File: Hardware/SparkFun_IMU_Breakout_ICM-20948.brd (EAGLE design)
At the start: 25.4 x 25.4 mm, 79 parts, among them U1 TXB0108DQSR, U2 9DoF IMU, U3 1.8V/100mA

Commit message: Swap TXB0108 for TXS0108 - still needs last check, design review, and finalization
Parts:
- removed U$3: (no value), buzzard_labels_2:GND4
- added U$30, U$44: (no value), buzzard_labels_2:VIN5
- U1: value TXB0108DQSR -> -VFQFN_20; device SparkFun-IC-Comms:UFDFN-20 -> SparkFun-IC-Comms:VFQFN-20
- moved C3 5.76 mm to (7.92, 12.7), turned to 90 degrees
- moved U1 0.89 mm to (12.7, 7.24)
- moved JP4 0.77 mm to (15.7, 7.87)
- moved U$25 0.77 mm to (15.7, 8.38)
- moved C1 0.51 mm to (9.40, 12.7)
- moved R1 0.38 mm to (18.3, 19.2)
- moved R3 0.38 mm to (19.8, 19.2)
- moved R5 0.38 mm to (7.11, 19.2)
- moved R6 0.38 mm to (5.59, 19.2)
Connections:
- net 1.8V: now also U1.10, U1.2; no longer U1.5, U1.6
- net AD0/SDO: now also U1.3; no longer U1.2
- net AD0/SDO_VIN: now also U1.18; no longer U1.19
- net AUX_CL: now also U1.7; no longer U1.8
- net AUX_CL_VIN: now also U1.14; no longer U1.13
- net AUX_DA: now also U1.6; no longer U1.7
- net AUX_DA_VIN: now also U1.15; no longer U1.14
- net FSYNC: now also U1.8; no longer U1.9
- net FSYNC_VIN: now also U1.13; no longer U1.12
- net GND: now also U1.11; no longer J4.6, U1.15
- net INT: now also U1.9; no longer U1.10
- net INT_VIN: now also U1.12; no longer U1.11
- net SCL/SCLK: now also U1.4; no longer U1.3
- net SCL/SCLK_VIN: now also U1.17; no longer U1.18
- net SDA/SDI: now also U1.5; no longer U1.4
- net SDA/SDI_VIN: now also U1.16; no longer U1.17
- net VIN: now also J4.6, U1.19; no longer U1.16
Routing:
- net VIN: track 72.7 -> 82.9 mm, vias 7 -> 6
- net FSYNC: track 12.0 -> 4.90 mm
- net AD0/SDO: track 13.7 -> 7.35 mm
- net GND: track 17.5 -> 11.8 mm, vias 26 -> 29
- net !CS: track 19.1 -> 13.7 mm
- net N$1: track 2.00 -> 7.02 mm
- net INT: track 11.0 -> 8.04 mm
- net AUX_DA: track 18.0 -> 20.3 mm
- net AD0/SDO_VIN: track 18.8 -> 20.5 mm, vias 1 -> 3
- net SCL/SCLK_VIN: track 37.2 -> 35.6 mm, vias 1 -> 3
- net AUX_CL: track 11.0 -> 9.42 mm
- net !CS!_VIN: track 22.5 -> 23.9 mm, vias 4 -> 2
- net SDA/SDI: track 20.1 -> 21.2 mm, vias 2 -> 0
- net 1.8V: track 35.5 -> 36.2 mm, vias 4 -> 3
- net AUX_CL_VIN: track 39.9 -> 40.4 mm
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
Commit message: v20
v20 is intended to fix the I2C communications. We've identified that the TXB0108 logic level translation IC was unable to drive open-drain busses. To address this we've replaced that IC with the TXS0108 - a very similar chip that IS able to drive open-drain busses.
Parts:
- added TP1: 1.8V, SparkFun-Connectors:PAD.03X.03
- U1: value -VFQFN_20 -> TXS0108
- moved C4 0.13 mm to (12.7, 16.6)
- moved U3 0.13 mm to (12.7, 18.7)
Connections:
- net 1.8V: now also TP1.P$1
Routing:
- net !CS!_VIN: track 23.9 -> 22.6 mm
- net SDA/SDI_VIN: track 39.7 -> 38.5 mm, vias 3 -> 4
- net SCL/SCLK_VIN: track 35.6 -> 36.3 mm
- net SDA/SDI: track 21.2 -> 20.5 mm
- net SCL/SCLK: track 18.7 -> 18.1 mm
- net GND: track 11.8 -> 11.9 mm, vias 29 -> 33
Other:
- board text added: "v20"
- board text removed: "v10"

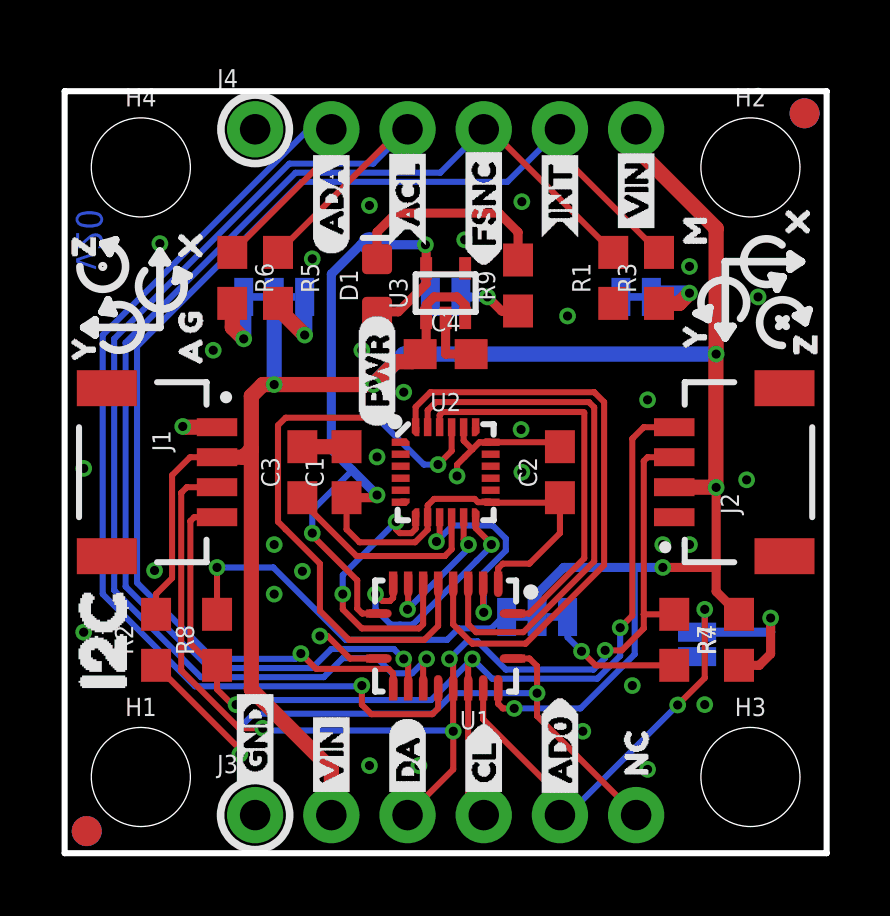
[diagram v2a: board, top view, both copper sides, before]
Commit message: Post design review changes for v20
- PWR silk changed to text only
- Moved P1 indicator on ICM-20948
- I<sup>2<\sup>C
- AD0 -> ADR
- No more '0' label for ADR
- Vin range double checked
- GND label on top left
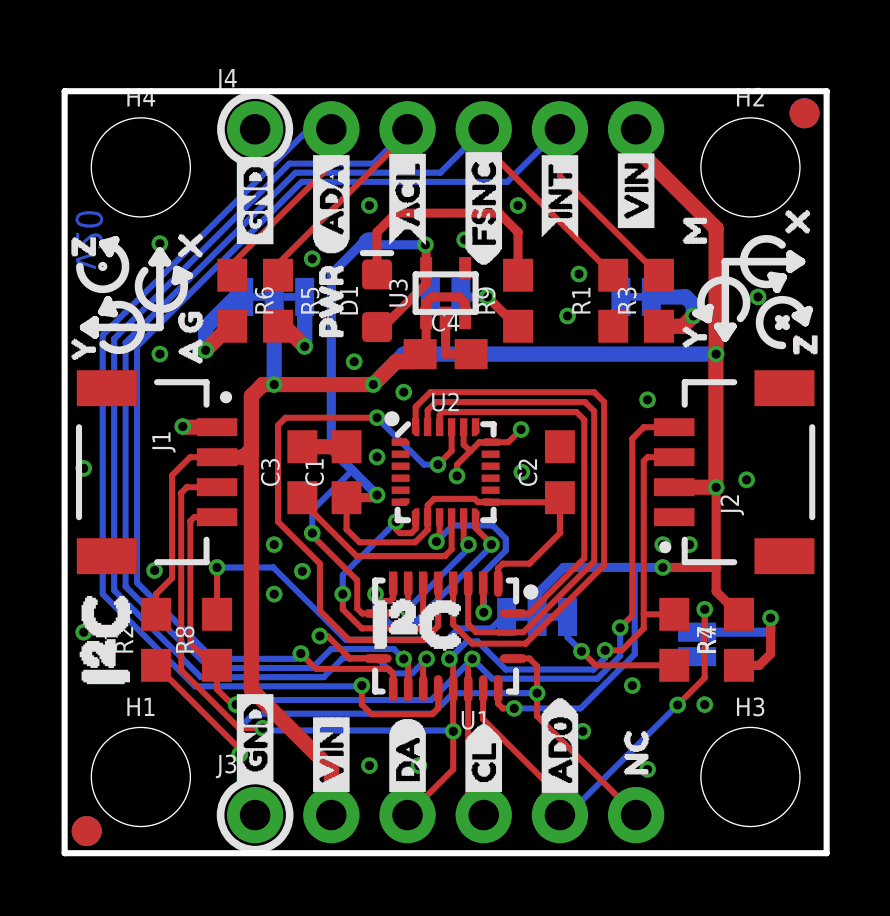
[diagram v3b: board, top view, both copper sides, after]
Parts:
- removed U$32: (no value), buzzard_labels_2:#0#25
- added U$3: (no value), buzzard_labels_4:PWR0
- added U$45: (no value), buzzard_labels_4:I#C1
- JP2: value AD0 -> ADR
- U$23: device buzzard_labels_2:I2C18 -> buzzard_labels_4:ADR2
- U$24: device buzzard_labels_2:AD020 -> buzzard_labels_2:GND4
- U$33: device buzzard_labels (1):PWR0 -> buzzard_labels_4:I#C1
- moved U$23 20.1 mm to (21.1, 7.49), flipped to the bottom
- moved U$24 19.2 mm to (6.35, 19.9), flipped to the top
- moved U$33 6.75 mm to (8.89, 7.62), turned to 0 degrees
- moved R1 0.76 mm to (18.3, 18.4)
- moved R3 0.76 mm to (19.8, 18.4)
- moved R5 0.76 mm to (7.11, 18.4)
- moved R6 0.76 mm to (5.59, 18.4)
- moved D1 0.51 mm to (10.4, 18.4)
- moved R9 0.51 mm to (15.1, 18.4)
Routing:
- net GND: track 11.9 -> 10.8 mm
- net N$9: track 7.05 -> 8.07 mm
- net N$7: track 2.74 -> 3.70 mm
- net INT_VIN: track 40.9 -> 41.7 mm
- net AUX_DA_VIN: track 38.5 -> 39.3 mm
- net FSYNC_VIN: track 40.9 -> 41.6 mm
- net AUX_CL_VIN: track 40.4 -> 41.1 mm
- net N$8: track 2.55 -> 3.17 mm
